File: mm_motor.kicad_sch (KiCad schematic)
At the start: 1 part, among them M1 N20_encoder

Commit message: tp2
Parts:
- added C7: 2.2uF 16V, symbol Device:C_Small
- added J3: Conn_01x06, symbol Connector_Generic:Conn_01x06
- added R8 (x2): 100, Resistor_SMD:R_0603_1608Metric, symbol Device:R
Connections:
- net C1: now also R8.1
- net C2: now also R8.1
- net MA: now also J3.1 (Pin_1)
- net MB: now also J3.6 (Pin_6)
- new net: J3.4 (Pin_4), R8.2
- new net: J3.3 (Pin_3), R8.2
- new net +BATT: C7.1, J3.2 (Pin_2)
- new net GND: C7.2, J3.5 (Pin_5)
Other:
- moved on the sheet: M1

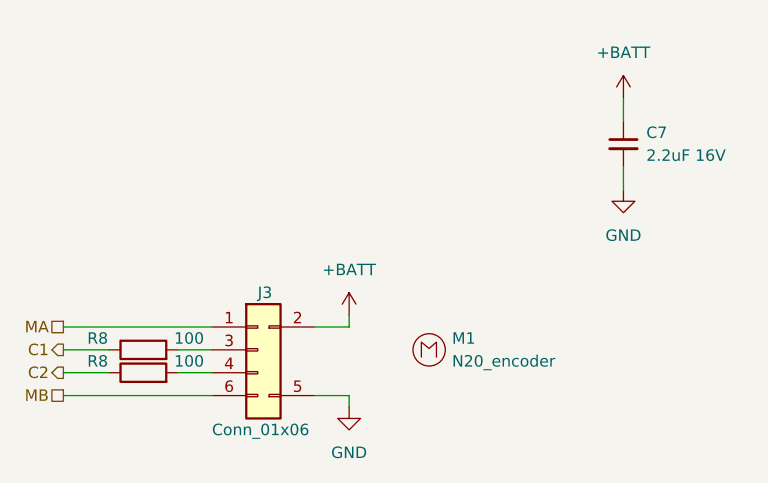
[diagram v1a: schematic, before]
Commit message: updated to kicad 8.0
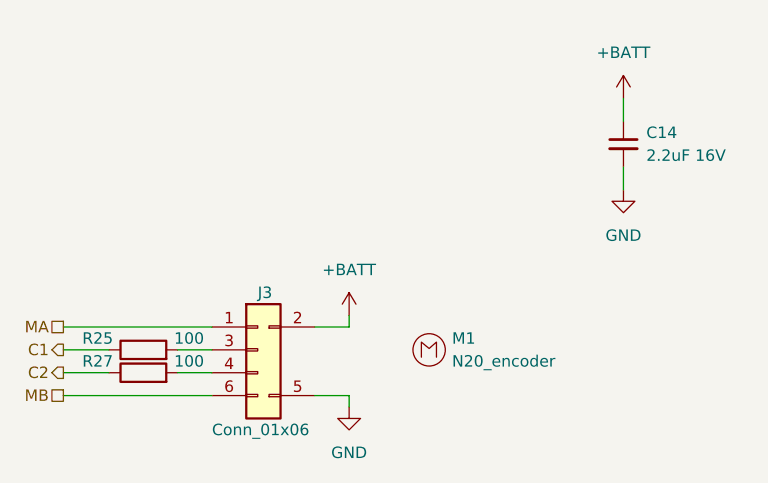
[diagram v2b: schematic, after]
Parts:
- renumbered C7 to C14, R8 to R25, R8 to R27
